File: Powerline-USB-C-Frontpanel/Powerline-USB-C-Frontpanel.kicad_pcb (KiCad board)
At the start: 2 copper layers, 15 x 128.5 mm, 6 parts

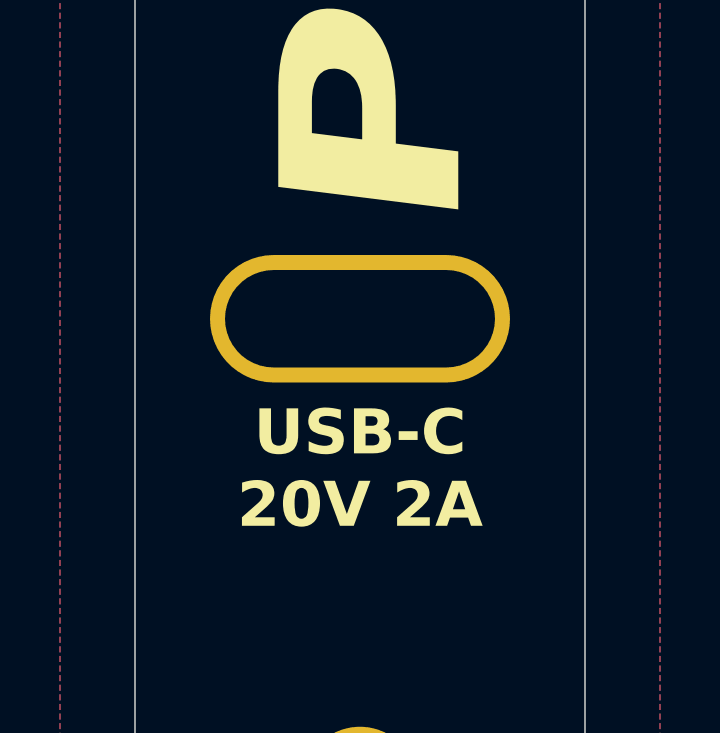
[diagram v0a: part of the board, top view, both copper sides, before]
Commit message: update to kicad9
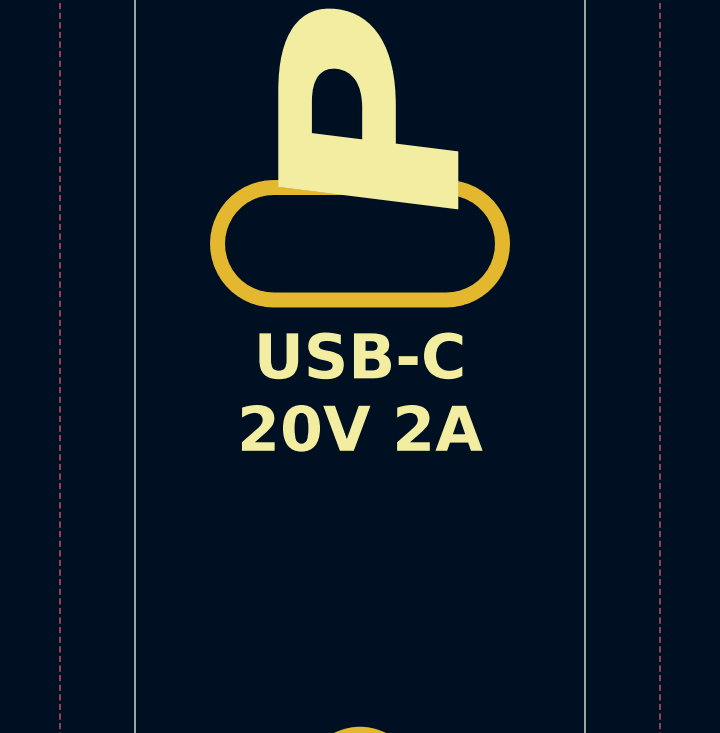
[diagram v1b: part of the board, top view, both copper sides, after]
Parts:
- moved H6 2.25 mm to (80.0, 122.0)
